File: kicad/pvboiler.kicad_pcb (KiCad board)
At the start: 2 copper layers, 125 x 60 mm, 36 parts, among them J1 Conn_01x04, J2 Screw_Terminal_01x04, J3 Conn_01x04, J4 Screw_Terminal_01x03, U1 MOC3021M, U2 H11AA1, U3 IRM-03-5

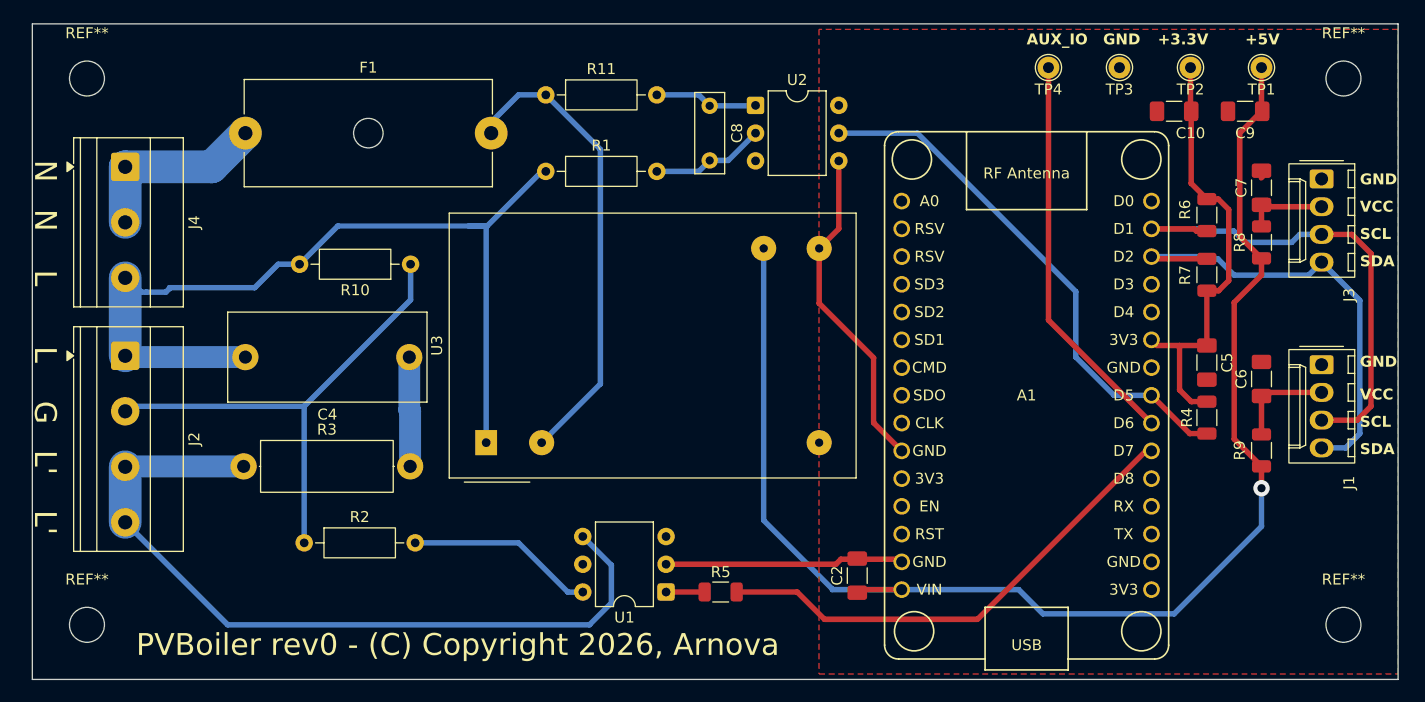
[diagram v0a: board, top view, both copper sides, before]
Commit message: changed: Increase opto cap size footprint changed: Pcb version bump to rev1
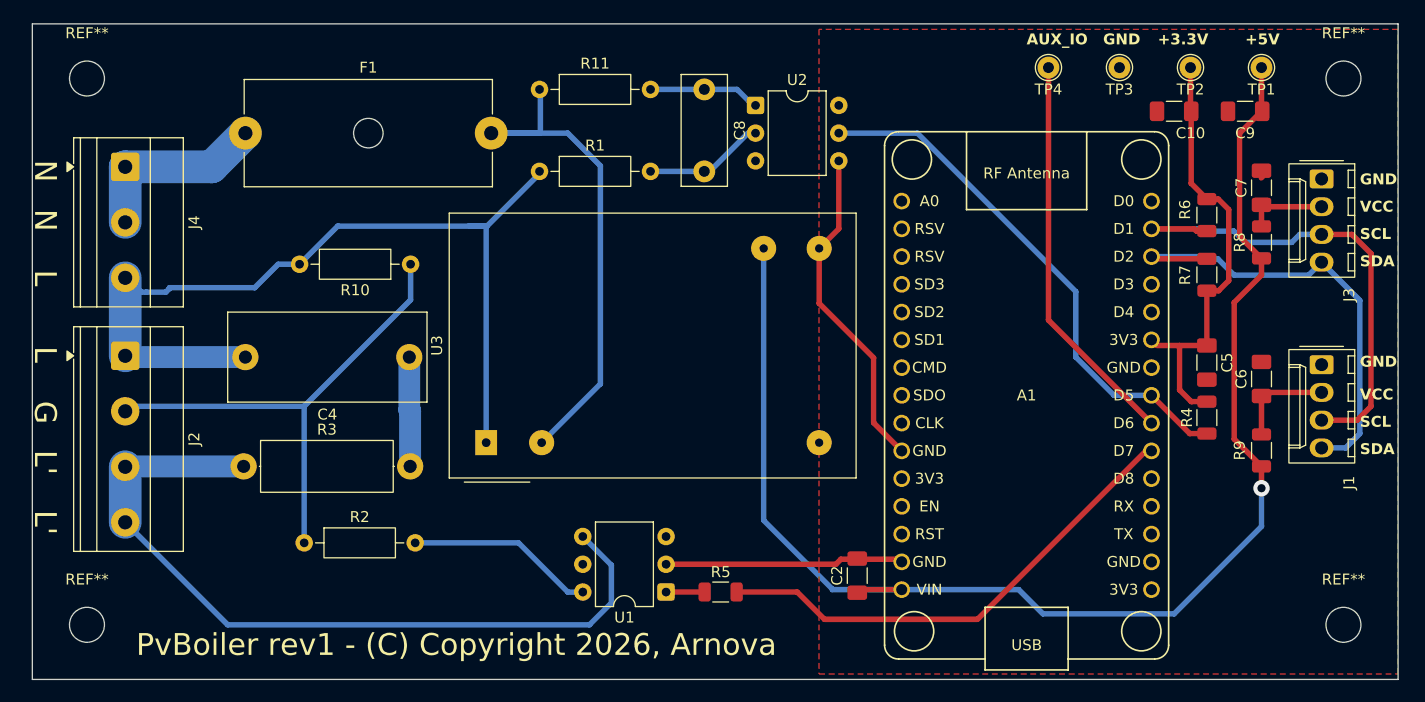
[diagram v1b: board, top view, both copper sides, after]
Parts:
- A1: value NodeMCUv2-Amica -> NodeMCUv2_Amica
- C8: footprint Capacitor_THT:C_Rect_L7.2mm_W2.5mm_P5.00mm -> Capacitor_THT:C_Rect_L10.0mm_W4.0mm_P7.50mm_MKS4
- moved C8 1.58 mm to (76.5, 41.0)
- moved R11 0.76 mm to (61.4, 41.0)
- moved R1 0.57 mm to (61.4, 48.5)
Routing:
- net Net-(U3-AC/N): track 43.7 -> 47.3 mm
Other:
- board text added: "PvBoiler rev1 - (C) Copyright 2026, Arnova"
- board text removed: "PVBoiler rev0 - (C) Copyright 2026, Arnova"
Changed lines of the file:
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@@
 	(footprint "Resistor_THT:R_Axial_DIN0207_L6.3mm_D2.5mm_P10.16mm_Horizontal"
 		(layer "F.Cu")
-		(at 61.995 41.5)
+		(at 61.42 41)
 		(descr "Resistor, Axial_DIN0207 series, Axial, Horizontal, pin pitch=10.16mm, 0.25W = 1/4W, length*diameter=6.3*2.5mm^2, http://cdn-reichelt.de/documents/datenblatt/B400/1_4W%23YAG.pdf")
 		(tags "Resistor Axial_DIN0207 series Axial Horizontal pin pitch 10.16mm 0.25W = 1/4W length 6.3mm diameter 2.5mm")
@@
 			)
 		)
-		(property "Value" "NodeMCUv2-Amica"
+		(property "Value" "NodeMCUv2_Amica"
 			(at -0.43 -5.08 0)
 			(layer "F.Fab")
@@
 		(sheetname "/")
 		(sheetfile "pvboiler.kicad_sch")
+		(units
+			(unit
+				(name "A")
+				(pins "1" "2" "3" "4" "5" "6" "7" "8" "9" "10" "11" "12" "13" "14" "15"
+					"30" "29" "28" "27" "26" "25" "24" "23" "22" "21" "20" "19" "18" "17"
+					"16"
+				)
+			)
+		)
 		(attr through_hole)
 		(duplicate_pad_numbers_are_jumpers no)
@@
 	(footprint "Resistor_THT:R_Axial_DIN0207_L6.3mm_D2.5mm_P10.16mm_Horizontal"
 		(layer "F.Cu")
-		(at 61.995 48.5)
+		(at 61.42 48.5)
 		(descr "Resistor, Axial_DIN0207 series, Axial, Horizontal, pin pitch=10.16mm, 0.25W = 1/4W, length*diameter=6.3*2.5mm^2, http://cdn-reichelt.de/documents/datenblatt/B400/1_4W%23YAG.pdf")
 		(tags "Resistor Axial_DIN0207 series Axial Horizontal pin pitch 10.16mm 0.25W = 1/4W length 6.3mm diameter 2.5mm")
@@
 		)
 	)
-	(footprint "Capacitor_THT:C_Rect_L7.2mm_W2.5mm_P5.00mm"
+	(footprint "Capacitor_THT:C_Rect_L10.0mm_W4.0mm_P7.50mm_MKS4"
 		(layer "F.Cu")
-		(at 76.995 42.5 -90)
-		(descr "C, Rect series, Radial, pin pitch=5.00mm, length*width=7.2*2.5mm^2, Capacitor, R82, https://content.kemet.com/datasheets/KEM_F3101_R82.pdf")
-		(tags "C Rect series Radial pin pitch 5.00mm length 7.2mm width 2.5mm Capacitor R82")
+		(at 76.5 41 -90)
+		(descr "C, Rect series, Radial, pin pitch=7.50mm, length*width=10*4.0mm^2, Capacitor, http://www.wima.com/EN/WIMA_MKS_4.pdf")
+		(tags "C Rect series Radial pin pitch 7.50mm length 10mm width 4.0mm Capacitor")
 		(property "Reference" "C8"
-			(at 2.5 -2.5 270)
+			(at 3.75 -3.25 270)
 			(layer "F.SilkS")
 			(effects
@@
 		)
 		(property "Value" "1nF 285VAC (Optional)"
-			(at 2.5 2.5 270)
+			(at 3.75 3.25 270)
 			(layer "F.Fab")
 			(effects
@@
 		(duplicate_pad_numbers_are_jumpers no)
 		(fp_line
-			(start -1.22 1.37)
-			(end -1.22 -1.37)
+			(start -1.37 2.12)
+			(end -1.37 -2.12)
 			(stroke
 				(width 0.12)
@@
 		)
 		(fp_line
-			(start 6.22 1.37)
-			(end -1.22 1.37)
+			(start 8.87 2.12)
+			(end -1.37 2.12)
 			(stroke
 				(width 0.12)
@@
 		)
 		(fp_line
-			(start -1.22 -1.37)
-			(end 6.22 -1.37)
+			(start -1.37 -2.12)
+			(end 8.87 -2.12)
 			(stroke
 				(width 0.12)
@@
 		)
 		(fp_line
-			(start 6.22 -1.37)
-			(end 6.22 1.37)
+			(start 8.87 -2.12)
+			(end 8.87 2.12)
 			(stroke
 				(width 0.12)
@@
 		)
 		(fp_rect
-			(start -1.35 -1.5)
-			(end 6.35 1.5)
+			(start -1.5 -2.25)
+			(end 9 2.25)
 			(stroke
 				(width 0.05)
@@
 		)
 		(fp_rect
-			(start -1.1 -1.25)
-			(end 6.1 1.25)
+			(start -1.25 -2)
+			(end 8.75 2)
 			(stroke
 				(width 0.1)
@@
 		)
 		(fp_text user "${REFERENCE}"
-			(at 2.5 0 270)
+			(at 3.75 0 270)
 			(layer "F.Fab")
 			(effects
@@
 		(pad "1" thru_hole circle
 			(at 0 0 270)
-			(size 1.5 1.5)
-			(drill 0.75)
+			(size 2 2)
+			(drill 1)
 			(layers "*.Cu" "*.Mask")
 			(remove_unused_layers no)
@@
 		)
 		(pad "2" thru_hole circle
-			(at 5 0 270)
-			(size 1.5 1.5)
-			(drill 0.75)
+			(at 7.5 0 270)
+			(size 2 2)
+			(drill 1)
 			(layers "*.Cu" "*.Mask")
 			(remove_unused_layers no)
@@
 		)
 		(embedded_fonts no)
-		(model "${KICAD10_3DMODEL_DIR}/Capacitor_THT.3dshapes/C_Rect_L7.2mm_W2.5mm_P5.00mm.step"
+		(model "${KICAD10_3DMODEL_DIR}/Capacitor_THT.3dshapes/C_Rect_L10.0mm_W4.0mm_P7.50mm_MKS4.step"
 			(offset
 				(xyz 0 0 0)
@@
 		)
 	)
-	(gr_text "PVBoiler rev0 - (C) Copyright 2026, Arnova"
+	(gr_text "PvBoiler rev1 - (C) Copyright 2026, Arnova\n"
 		(at 24.5 93 0)
 		(layer "F.SilkS")
@@
 	)
 	(segment
-		(start 66.995 46.5)
-		(end 66.995 67.95)
+		(start 57 45)
+		(end 61.5 45)
 		(width 0.5)
 		(layer "B.Cu")
@@
 	)
 	(segment
-		(start 66.995 67.95)
-		(end 61.615 73.33)
+		(start 57 45)
+		(end 64 45)
 		(width 0.5)
 		(layer "B.Cu")
@@
 	)
 	(segment
-		(start 61.995 41.5)
-		(end 66.995 46.5)
+		(start 66.995 47.995)
+		(end 66.995 67.95)
 		(width 0.5)
 		(layer "B.Cu")
@@
 	)
 	(segment
-		(start 57 44)
-		(end 59.5 41.5)
+		(start 61.5 45)
+		(end 61.5 41)
 		(width 0.5)
 		(layer "B.Cu")
@@
 	)
 	(segment
-		(start 59.5 41.5)
-		(end 62.5 41.5)
+		(start 64 45)
+		(end 66.995 47.995)
 		(width 0.5)
 		(layer "B.Cu")
@@
 	)
 	(segment
-		(start 57 45)
-		(end 57 44)
+		(start 66.995 67.95)
+		(end 61.615 73.33)
 		(width 0.5)
 		(layer "B.Cu")
@@
 	)
 	(segment
-		(start 75.995 41.5)
-		(end 72.155 41.5)
+		(start 81.19 42.46)
+		(end 81.15 42.5)
 		(width 0.5)
 		(layer "B.Cu")
@@
 	)
 	(segment
-		(start 76.995 42.5)
-		(end 81.15 42.5)
+		(start 81.15 42.5)
+		(end 81 42.5)
 		(width 0.5)
 		(layer "B.Cu")
@@
 	)
 	(segment
-		(start 76.995 42.5)
-		(end 75.995 41.5)
+		(start 79.5 41)
+		(end 77 41)
 		(width 0.5)
 		(layer "B.Cu")
@@
 	)
 	(segment
-		(start 81.15 42.5)
-		(end 81.19 42.46)
+		(start 81 42.5)
+		(end 79.5 41)
+		(width 0.5)
+		(layer "B.Cu")
+		(net "Net-(C8-Pad1)")
+	)
+	(segment
+		(start 77 41)
+		(end 72.155 41)
 		(width 0.5)
 		(layer "B.Cu")
@@
 	)
 	(segment
+		(start 55 53.5)
+		(end 56.625 53.5)
+		(width 0.5)
+		(layer "B.Cu")
+		(net "/230VAC_L")
+	)
+	(segment
 		(start 23.5 59.14622)
 		(end 24.56066 59.14622)
@@
 	)
 	(segment
+		(start 61.42 48.705)
+		(end 61.42 48.5)
+		(width 0.5)
+		(layer "B.Cu")
+		(net "/230VAC_L")
+	)
+	(segment
 		(start 23.5 58.245)
 		(end 23.5 65.38)
@@
 	)
 	(segment
-		(start 55 53.5)
-		(end 56.625 53.5)
-		(width 0.5)
-		(layer "B.Cu")
-		(net "/230VAC_L")
-	)
-	(segment
-		(start 56.625 53.5)
-		(end 61.625 48.5)
-		(width 0.5)
-		(layer "B.Cu")
-		(net "/230VAC_L")
-	)
-	(segment
 		(start 27.227817 59.55)
 		(end 27.55 59.227817)
@@
 	)
 	(segment
-		(start 61.625 48.5)
-		(end 61.995 48.5)
+		(start 56.625 53.5)
+		(end 61.42 48.705)
 		(width 0.5)
 		(layer "B.Cu")
@@
 	)
 	(segment
-		(start 76.995 47.5)
-		(end 78.69 47.5)
+		(start 77 48.5)
+		(end 80.5 45)
 		(width 0.5)
 		(layer "B.Cu")
@@
 	)
 	(segment
-		(start 78.69 47.5)
+		(start 80.5 45)
 		(end 81.19 45)
 		(width 0.5)
@@
 	)
 	(segment
-		(start 75.995 48.5)
-		(end 72.155 48.5)
-		(width 0.5)
-		(layer "B.Cu")
-		(net "Net-(C8-Pad2)")
-	)
-	(segment
-		(start 76.995 47.5)
-		(end 75.995 48.5)
+		(start 72.155 48.5)
+		(end 77 48.5)
 		(width 0.5)
 		(layer "B.Cu")

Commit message: updated: Some tweaks in KiCAD schematic / pcb
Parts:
- added R12: 22E, Resistor_SMD:R_1206_3216Metric, F.Cu at (132.5, 63.5)
- added R13: 22E, Resistor_SMD:R_1206_3216Metric, F.Cu at (132.5, 60.5)
- added R14: 22E, Resistor_SMD:R_1206_3216Metric, F.Cu at (132.5, 69.5)
- added R15: 22E, Resistor_SMD:R_1206_3216Metric, F.Cu at (132.5, 66.5)
- R6, R7: value 10K -> 2K2
- R8, R9: value 0E -> 10E
- moved C6 7.00 mm to (127.5, 74.5)
- moved J1 7.00 mm to (133.0, 73.2)
- moved R9 7.00 mm to (127.5, 81.0)
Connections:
- J1 pad 3: /I2C_SCL -> Net-(J1-Pin_3)
- J1 pad 4: /I2C_SDA -> Net-(J1-Pin_4)
- J3 pad 3: /I2C_SCL -> Net-(J3-Pin_3)
- J3 pad 4: /I2C_SDA -> Net-(J3-Pin_4)
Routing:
- net Net-(J1-Pin_4): track 0.00 -> 18.5 mm
- net /I2C_SDA: track 43.1 -> 29.0 mm, vias 0 -> 1
- net /I2C_SCL: track 46.0 -> 32.1 mm, vias 0 -> 1
- net Net-(J3-Pin_3): track 0.00 -> 12.5 mm
- net Net-(J1-Pin_3): track 0.00 -> 10.5 mm
- net +5V: track 128.3 -> 134.4 mm, vias 1 -> 3
- net Net-(J3-Pin_4): track 0.00 -> 4.09 mm

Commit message: changed: Expose ESP8266 D0 on extra tp
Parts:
- added R16: 4K7, Resistor_SMD:R_1206_3216Metric, F.Cu at (122.5, 51.0)
- added R17: 4K7, Resistor_SMD:R_1206_3216Metric, F.Cu at (122.5, 72.5)
- added TP5: TestPoint, TestPoint:TestPoint_THTPad_D2.0mm_Drill1.0mm, F.Cu at (108.0, 39.0)
- moved TP4 6.50 mm to (101.5, 39.0)
- moved R6 1.46 mm to (122.5, 56.5), turned to 0 degrees
- moved R4 1.04 mm to (122.5, 70.0), turned to 0 degrees
- moved R7 1.00 mm to (122.5, 53.5), turned to 0 degrees
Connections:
- A1 pad 22: /AUX_GPIO -> /ONE_WIRE
- A1 pad 30: unconnected-(A1-D0-Pad30) -> /AUX_GPIO
- TP4 pad 1: /AUX_GPIO -> /ONE_WIRE
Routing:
- net /ONE_WIRE: track 0.00 -> 43.1 mm
- net /AUX_GPIO: track 36.4 -> 20.5 mm
- net /ZERO_CROSS: track 48.6 -> 46.7 mm
- net +3.3V_1: track 41.8 -> 43.7 mm
- net /I2C_SDA: track 29.0 -> 27.5 mm
- net /I2C_SCL: track 32.1 -> 30.7 mm
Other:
- board text added: "1-WIRE"

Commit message: changed: Add (future) CT connection for A0 changed: Improve schematic
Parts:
- added C1: 10uF, Capacitor_Tantalum_SMD:CP_EIA-3216-18_Kemet-A_HandSolder, F.Cu at (100.0, 43.0)
- added R18: 100E (Optional), Resistor_SMD:R_1206_3216Metric, F.Cu at (94.5, 43.0)
- added R19: 68K, Resistor_SMD:R_1206_3216Metric, F.Cu at (89.5, 78.5)
- added R20: 68K, Resistor_SMD:R_1206_3216Metric, F.Cu at (89.5, 81.5)
- added TP6: TestPoint, TestPoint:TestPoint_THTPad_D2.0mm_Drill1.0mm, F.Cu at (88.5, 39.0)
- added TP7: TestPoint, TestPoint:TestPoint_THTPad_D2.0mm_Drill1.0mm, F.Cu at (95.0, 39.0)
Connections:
- A1 pad 1: unconnected-(A1-A0-Pad1) -> /CT1
- A1 pad 11: unconnected-(A1-3.3V-Pad11) -> /+3.3V_3
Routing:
- net /CT2: track 0.00 -> 59.5 mm, vias 0 -> 1
- net GND: track 52.4 -> 22.0 mm
- net /CT1: track 0.00 -> 16.2 mm
- net /+3.3V_3: track 0.00 -> 4.39 mm
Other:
- board text added: "AUX-IO"
- board text added: "CT Clamp"
- board text removed: "AUX_IO"

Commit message: updated: Tweaks in schematic/PCB
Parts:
- added R21: 10E, Resistor_SMD:R_1206_3216Metric, F.Cu at (129.5, 44.5)
- added R22: 10E, Resistor_SMD:R_1206_3216Metric, F.Cu at (121.0, 44.5)
- added R23: 100E, Resistor_SMD:R_1206_3216Metric, F.Cu at (107.0, 43.0)
- R16, R17: value 4K7 -> 2K2
- moved C10 3.50 mm to (116.0, 43.0)
- moved C9 1.58 mm to (125.5, 44.5), turned to -90 degrees
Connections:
- C10 pad 1: +3.3V_1 -> Net-(C10-Pad1)
- C9 pad 1: +5V -> Net-(C9-Pad1)
- TP1 pad 1: +5V -> Net-(C9-Pad1)
- TP2 pad 1: +3.3V_1 -> Net-(C10-Pad1)
- TP4 pad 1: /ONE_WIRE -> Net-(R23-Pad2)
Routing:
- net Net-(C9-Pad1): track 0.00 -> 8.91 mm
- net Net-(C10-Pad1): track 0.00 -> 7.49 mm
- net +3.3V_1: track 43.7 -> 37.0 mm
- net /ONE_WIRE: track 43.1 -> 36.6 mm
- net Net-(R23-Pad2): track 0.00 -> 5.69 mm
- net /AUX_GPIO: track 20.5 -> 19.8 mm
- net +5V: track 134.4 -> 133.7 mm
